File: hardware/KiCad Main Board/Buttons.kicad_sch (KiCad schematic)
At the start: 67 parts, among them SW3 RotaryEncoder_Switch, U11 P091S-FC20BR10k

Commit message: working on PCB
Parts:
- removed D10, D11, D12, D13, D14, D15, D16, D17, D18, D19, D20, D21, D22, D23, D24, D25, D27, D28, D29, D30, D8, D9: 1N4148, symbol Device:D_Small
- added D10, D11, D12, D13, D14, D15, D16, D17, D18, D19, D20, D21, D22, D23, D24, D25, D27, D28, D29, D4, D8, D9: 1N4148WS, Diode_SMD:D_SOD-323, symbol Diode:1N4148WS
- D32: footprint (none) -> Diode_SMD:D_0603_1608Metric_Pad1.05x0.95mm_HandSolder
- R21, R22, R24, R40, R51: footprint (none) -> Resistor_SMD:R_0603_1608Metric_Pad0.98x0.95mm_HandSolder
- SW3: value RotaryEncoder_Switch -> PEC12R-21xx-S0012; footprint (none) -> Rotary_Encoder:RotaryEncoder_Bourns_Horizontal_PEC12R-2x17F-Sxxxx
- SW_#1, SW_*1, SW_0, SW_1, SW_2, SW_3, SW_4, SW_5, SW_6, SW_7, SW_8, SW_9, SW_BACK1, SW_DOWN1, SW_ENTER1, SW_LEFT1, SW_RIGHT1, SW_UP1: value SW_Push -> TS-1187A-B-A-B; footprint (none) -> Button_Switch_SMD:SW_Push_1P1T_XKB_TS-1187A
- SW_PTT1, SW_SIDE1, SW_SIDE2: value SW_Push -> 1825027-8; footprint (none) -> Button_Switch_THT:SW_Tactile_SPST_Angled_PTS645Vx58-2LFS
- U11: footprint (none) -> P091S:P091S-FC20BR10K
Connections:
- net BTN_MTX_0: now also D24.1 (K), D25.1 (K), D27.1 (K), D28.1 (K)
- net BTN_MTX_1: now also D20.1 (K), D21.1 (K), D22.1 (K), D23.1 (K)
- net BTN_MTX_2: now also D13.1 (K), D14.1 (K), D15.1 (K), D16.1 (K)
- net BTN_MTX_3: now also D17.1 (K), D18.1 (K), D19.1 (K), D29.1 (K)
- net BTN_MTX_4: now also D10.1 (K), D11.1 (K), D12.1 (K)
- net BTN_MTX_5: now also D4.1 (K), D8.1 (K), D9.1 (K)
- net at SW_5.1: now also D18.2 (A)
- net at SW_RIGHT1.1: now also D27.2 (A)
- net at SW_3.1: now also D14.2 (A)
- net at SW_BACK1.1: now also D23.2 (A)
- net at SW_#1.1: now also D9.2 (A)
- net at SW_SIDE1.1: now also D20.2 (A)
- net at SW_PTT1.1: now also D28.2 (A)
- net at SW_LEFT1.1: now also D24.2 (A)
- net at SW_8.1: now also D11.2 (A)
- net at SW_1.1: now also D16.2 (A)
- net at SW_SIDE2.1: now also D13.2 (A)
- net at SW_ENTER1.1: now also D21.2 (A)
- net at SW_6.1: now also D19.2 (A)
- net at SW_4.1: now also D17.2 (A)
- net at SW_*1.1: now also D4.2 (A)
- net at SW_DOWN1.1: now also D22.2 (A)
- net at SW_UP1.1: now also D25.2 (A)
- net at SW3.S1: now also D29.2 (A)
- net at SW_7.1: now also D12.2 (A)
- net at SW_2.1: now also D15.2 (A)
- net at SW_0.1: now also D8.2 (A)
- net at SW_9.1: now also D10.2 (A)
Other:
- moved on the sheet: C81, C82, D46, D47, R21, R22, R24, R40, SW3, SW_#1, SW_*1, SW_0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

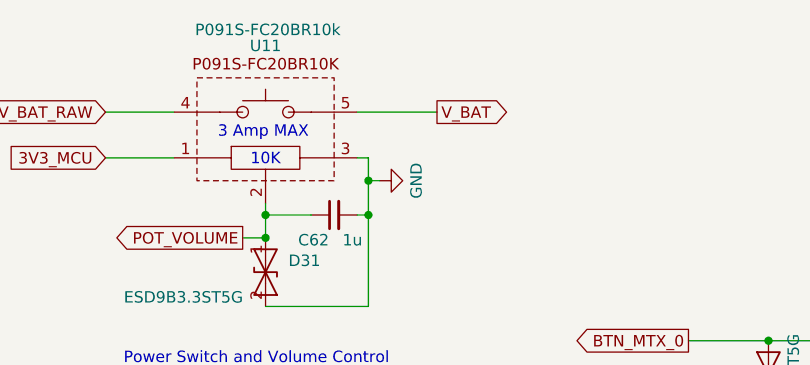
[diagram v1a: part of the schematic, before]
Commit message: all GPIO nets connected on schematic
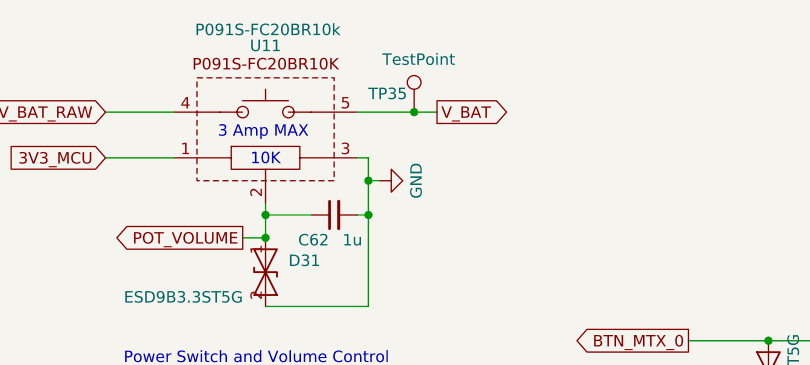
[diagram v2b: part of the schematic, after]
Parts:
- added TP35: TestPoint, TestPoint:TestPoint_Pad_D1.0mm, symbol Connector:TestPoint
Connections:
- net V_BAT: now also TP35.1
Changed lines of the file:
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@@
+	)
+	(junction
+		(at 71.12 41.91)
+		(diameter 0)
+		(color 0 0 0 0)
 	)
 	(junction
@@
 	(wire
 		(pts
+			(xy 71.12 41.91) (xy 64.77 41.91)
+		)
+		(stroke
+			(width 0)
+			(type default)
+		)
+	)
+	(wire
+		(pts
 			(xy 110.49 101.6) (xy 123.19 101.6)
 		)
@@
 	(wire
 		(pts
-			(xy 73.66 41.91) (xy 64.77 41.91)
+			(xy 73.66 41.91) (xy 71.12 41.91)
 		)
 		(stroke
@@
 					(unit 1)
 				)
+			)
+		)
+	)
+	(symbol
+		(lib_id "Connector:TestPoint")
+		(at 71.12 41.91 0)
+		(unit 1)
+		(exclude_from_sim no)
+		(in_bom yes)
+		(on_board yes)
+		(dnp no)
+		(property "Reference" "TP35"
+			(at 70.358 39.878 0)
+			(effects
+				(font
+					(size 1.27 1.27)
+				)
+				(justify right)
+			)
+		)
+		(property "Value" "TestPoint"
+			(at 75.692 36.068 0)
+			(effects
+				(font
+					(size 1.27 1.27)
+				)
+				(justify right)
+			)
+		)
+		(property "Footprint" "TestPoint:TestPoint_Pad_D1.0mm"
+			(at 76.2 41.91 0)
+			(effects
+				(font
+					(size 1.27 1.27)
+				)
+				(hide yes)
+			)
+		)
+		(property "Datasheet" "~"
+			(at 76.2 41.91 0)
+			(effects
+				(font
+					(size 1.27 1.27)
+				)
+				(hide yes)
+			)
+		)
+		(property "Description" "test point"
+			(at 71.12 41.91 0)
+			(effects
+				(font
+					(size 1.27 1.27)
+				)
+				(hide yes)
+			)
+		)
+		(pin "1"
+		)
+		(instances
+			(project "OSS Radio Hardware Design"
+				(path "/fd5c68a7-f5d0-4135-a258-bde3ebf63307/7b56df82-cc6a-450b-93ef-d87bc728ade2"
+					(reference "TP35")
+					(unit 1)
+				)

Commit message: mostly designed PCB
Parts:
- removed SW3: PEC12R-21xx-S0012, Rotary_Encoder:RotaryEncoder_Bourns_Horizontal_PEC12R-2x17F-Sxxxx, symbol Device:RotaryEncoder_Switch
- added SW1: PEC09-2120F-S0012, PEC09-2120F-S0012:PEC09-2120F-S0012, symbol Device:RotaryEncoder_Switch
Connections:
- net BTN_ENC_A: no longer D47.1 (A1)
- net BTN_ENC_B: no longer D46.1 (A1)
- net BTN_MTX_D: now also SW1.S2
- net GND: now also SW1.C
- net at D29.2 (A): now also SW1.S1
- net at R40.1: now also D46.1 (A1), SW1.B
- net at R24.2: now also D47.1 (A1), SW1.A
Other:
- moved on the sheet: C81, C82, D46, D47, R21, R22, R24, R40

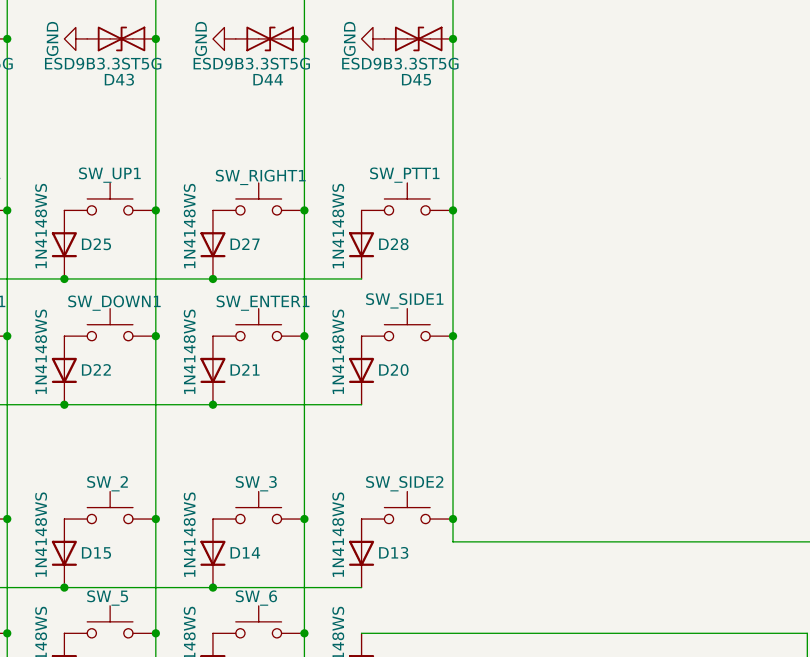
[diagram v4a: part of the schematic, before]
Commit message: wrote a quick test firmware and swapped PTT and Side2 buttons
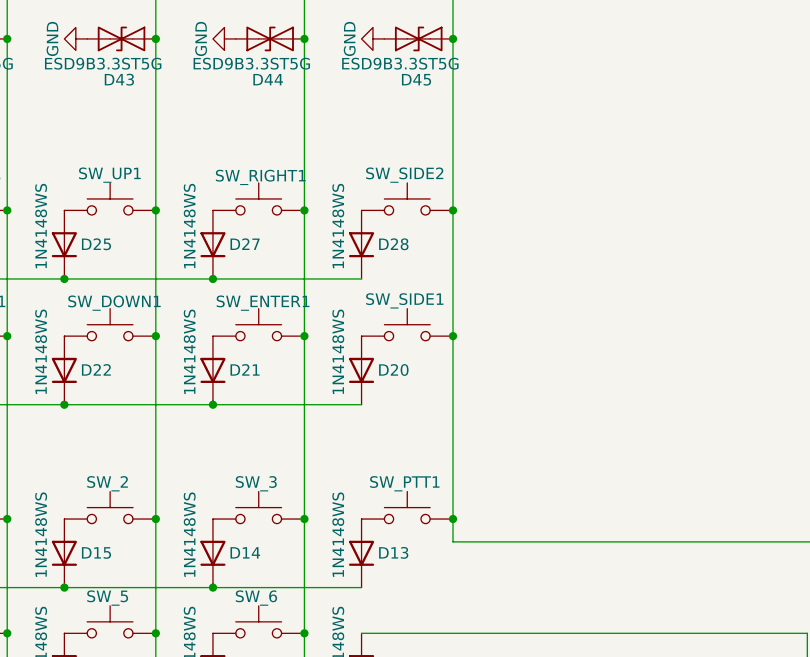
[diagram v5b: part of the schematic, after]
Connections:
- net at SW_PTT1.1: now also D13.2 (A); no longer D28.2 (A)
- net at SW_SIDE2.1: now also D28.2 (A); no longer D13.2 (A)
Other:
- moved on the sheet: SW_PTT1, SW_SIDE2
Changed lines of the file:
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@@
 	)
 	(junction
+		(at 182.88 93.98)
+		(diameter 0)
+		(color 0 0 0 0)
+	)
+	(junction
 		(at 227.33 134.62)
 		(diameter 0)
@@
 	)
 	(junction
-		(at 182.88 93.98)
+		(at 54.61 55.88)
 		(diameter 0)
 		(color 0 0 0 0)
 	)
 	(junction
-		(at 54.61 55.88)
+		(at 182.88 59.69)
 		(diameter 0)
 		(color 0 0 0 0)
@@
 	)
 	(junction
-		(at 182.88 59.69)
-		(diameter 0)
-		(color 0 0 0 0)
-	)
-	(junction
 		(at 245.11 127)
 		(diameter 0)
@@
 	(wire
 		(pts
+			(xy 182.88 93.98) (xy 182.88 96.52)
+		)
+		(stroke
+			(width 0)
+			(type default)
+		)
+	)
+	(wire
+		(pts
 			(xy 139.7 139.7) (xy 156.21 139.7)
 		)
@@
 	(wire
 		(pts
-			(xy 182.88 59.69) (xy 182.88 73.66)
+			(xy 182.88 40.64) (xy 182.88 59.69)
 		)
 		(stroke
@@
 	(wire
 		(pts
+			(xy 182.88 59.69) (xy 182.88 73.66)
+		)
+		(stroke
+			(width 0)
+			(type default)
+		)
+	)
+	(wire
+		(pts
 			(xy 101.6 81.28) (xy 104.14 81.28)
 		)
@@
 	(wire
 		(pts
-			(xy 182.88 40.64) (xy 182.88 59.69)
-		)
-		(stroke
-			(width 0)
-			(type default)
-		)
-	)
-	(wire
-		(pts
 			(xy 166.37 40.64) (xy 166.37 59.69)
 		)
@@
 	(wire
 		(pts
-			(xy 182.88 93.98) (xy 182.88 96.52)
-		)
-		(stroke
-			(width 0)
-			(type default)
-		)
-	)
-	(wire
-		(pts
 			(xy 123.19 114.3) (xy 139.7 114.3)
 		)
@@
 	(symbol
 		(lib_id "Switch:SW_Push")
-		(at 177.8 59.69 0)
+		(at 177.8 93.98 0)
 		(unit 1)
 		(exclude_from_sim no)
@@
 		(dnp no)
 		(property "Reference" "SW_PTT1"
-			(at 177.546 55.626 0)
+			(at 177.546 89.916 0)
 			(effects
 				(font
@@
 		)
 		(property "Value" "1825027-8"
-			(at 177.8 54.61 0)
+			(at 177.8 88.9 0)
 			(effects
 				(font
@@
 		)
 		(property "Footprint" "Button_Switch_THT:SW_Tactile_SPST_Angled_PTS645Vx58-2LFS"
-			(at 177.8 54.61 0)
+			(at 177.8 88.9 0)
 			(effects
 				(font
@@
 		)
 		(property "Datasheet" "~"
-			(at 177.8 54.61 0)
+			(at 177.8 88.9 0)
 			(effects
 				(font
@@
 		)
 		(property "Description" "Push button switch, generic, two pins"
-			(at 177.8 59.69 0)
+			(at 177.8 93.98 0)
 			(effects
 				(font
@@
 	(symbol
 		(lib_id "Switch:SW_Push")
-		(at 177.8 93.98 0)
+		(at 177.8 59.69 0)
 		(unit 1)
 		(exclude_from_sim no)
@@
 		(dnp no)
 		(property "Reference" "SW_SIDE2"
-			(at 177.546 89.916 0)
+			(at 177.546 55.626 0)
 			(effects
 				(font
@@
 		)
 		(property "Value" "1825027-8"
-			(at 177.8 88.9 0)
+			(at 177.8 54.61 0)
 			(effects
 				(font
@@
 		)
 		(property "Footprint" "Button_Switch_THT:SW_Tactile_SPST_Angled_PTS645Vx58-2LFS"
-			(at 177.8 88.9 0)
+			(at 177.8 54.61 0)
 			(effects
 				(font
@@
 		)
 		(property "Datasheet" "~"
-			(at 177.8 88.9 0)
+			(at 177.8 54.61 0)
 			(effects
 				(font
@@
 		)
 		(property "Description" "Push button switch, generic, two pins"
-			(at 177.8 93.98 0)
+			(at 177.8 59.69 0)
 			(effects
 				(font
